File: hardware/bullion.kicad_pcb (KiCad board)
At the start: 2 copper layers, 14 parts, among them IC1 ATMEGA328P-A, P1 USB_OTG, P2 CONN_01X07, U1 SJ1-3524NG, U2 CH340G, Y1 Crystal

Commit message: v2.
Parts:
- moved C7 94.2 mm to (146.5, 90.6)
- moved Y1 94.2 mm to (145.0, 86.4)
- moved C2 94.2 mm to (123.1, 96.3)
- moved C3 94.2 mm to (135.6, 87.5)
- moved C4 94.2 mm to (154.6, 88.0)
- moved C5 94.2 mm to (123.2, 103.6)
- moved C8 94.2 mm to (146.3, 106.0)
- moved IC1 94.2 mm to (144.1, 98.5)
- moved P1 94.2 mm to (128.1, 113.7)
- moved P2 94.2 mm to (136.2, 113.2)
- moved R1 94.2 mm to (153.7, 96.3)
- moved U1 94.2 mm to (159.1, 111.6)
- moved U2 94.2 mm to (128.4, 98.4)
- moved C1 94.0 mm to (134.0, 97.3)
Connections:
- P2 pad 1: +5V -> GND
- P2 pad 2: GND -> +5V
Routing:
- net GND: track 59.6 -> 48.0 mm, vias 7 -> 5
- net +5V: track 97.9 -> 108.7 mm
- net Net-(C2-Pad1): track 80.3 -> 84.3 mm

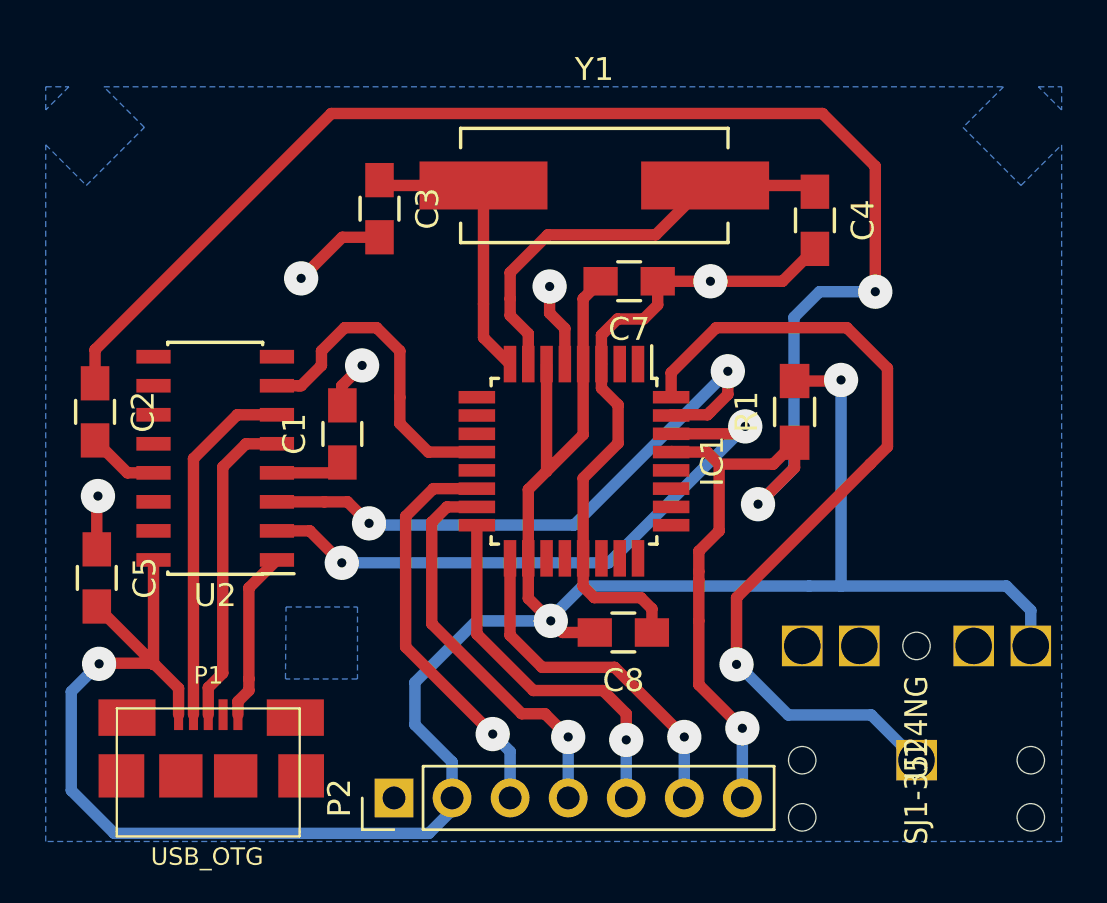
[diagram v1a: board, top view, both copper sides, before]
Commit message: Adding LEDs; fixing RS232 connection.
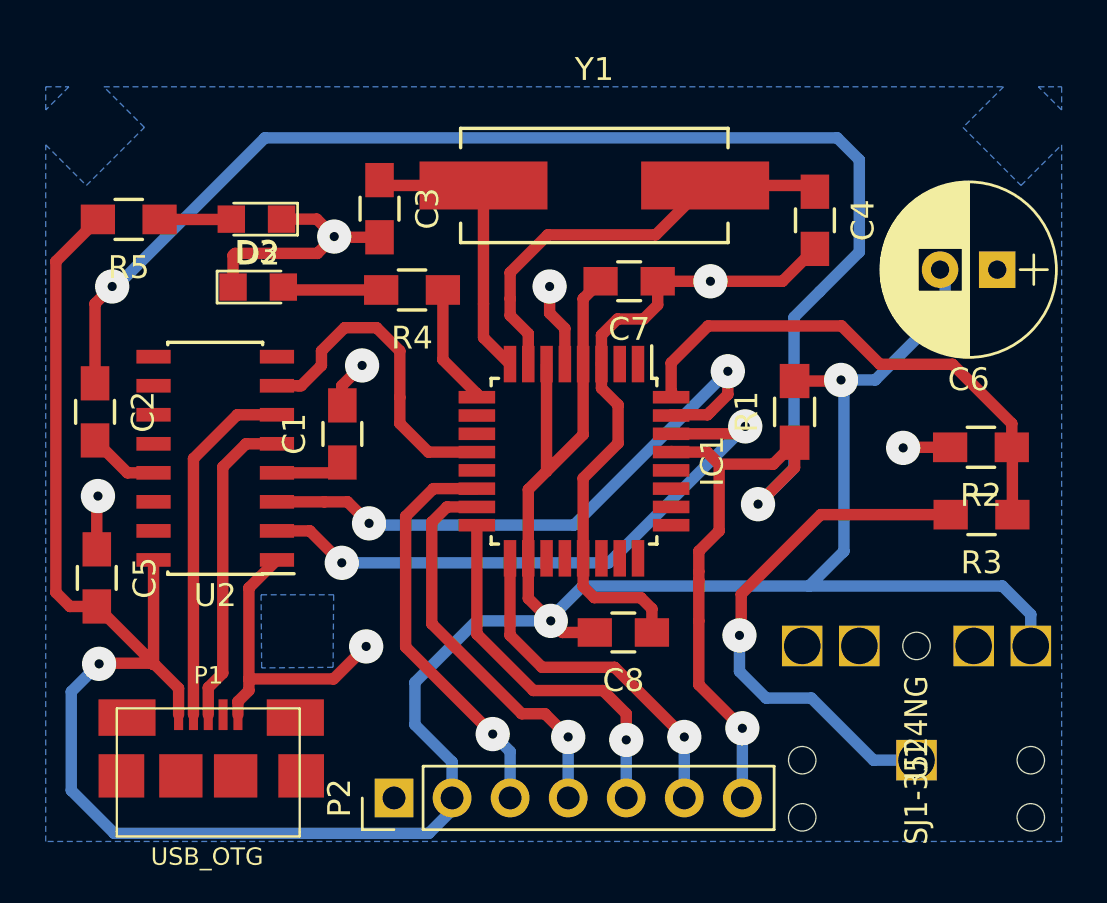
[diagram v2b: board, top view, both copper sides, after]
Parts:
- added C6: 47u, Capacitors_THT:CP_Radial_D7.5mm_P2.50mm, F.Cu at (162.6, 90.1)
- added D2: BLUE, LEDs:LED_0805, F.Cu at (130.3, 90.9)
- added D3: RED, LEDs:LED_0805, F.Cu at (130.2, 87.9)
- added R2: 2.2k, Resistors_SMD:R_0805_HandSoldering, F.Cu at (161.9, 97.9)
- added R3: 220, Resistors_SMD:R_0805_HandSoldering, F.Cu at (161.9, 100.8)
- added R4: 82, Resistors_SMD:R_0805_HandSoldering, F.Cu at (137.0, 91.0)
- added R5: 220, Resistors_SMD:R_0805_HandSoldering, F.Cu at (124.6, 87.9)
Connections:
- U1 pad 1: MM_TXD -> Net-(R3-Pad2)
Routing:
- net +5V: track 108.7 -> 136.0 mm
- net Net-(R3-Pad2): track 0.00 -> 23.4 mm, vias 0 -> 1
- net GND: track 48.0 -> 62.4 mm, vias 5 -> 7
- net MM_TXD: track 37.4 -> 23.1 mm, vias 1 -> 0
- net Net-(IC1-Pad9): track 0.00 -> 5.31 mm
- net Net-(D2-Pad2): track 0.00 -> 4.33 mm
- net Net-(D3-Pad2): track 0.00 -> 3.14 mm
- net Net-(C2-Pad1): track 84.3 -> 82.4 mm

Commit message: Updating hardware to latest revision; adding readme.
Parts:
- R5: value 220 -> 4.7k
- moved C6 2.31 mm to (160.3, 90.2), turned to 0 degrees
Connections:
- C6 pad 1: GND -> +5V
- C6 pad 2: +5V -> GND
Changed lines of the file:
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@@
   )
   (module Capacitors_THT:CP_Radial_D7.5mm_P2.50mm (layer F.Cu)
-    (at 162.6108 90.1192 180)
+    (at 160.2994 90.1954)
     (descr "CP, Radial series, Radial, pin pitch=2.50mm, , diameter=7.5mm, Electrolytic Capacitor")
     (tags "CP Radial series Radial pin pitch 2.50mm  diameter 7.5mm Electrolytic Capacitor")
-    (fp_text reference C6 (at 1.25 -4.81 180) (layer F.SilkS)
-      (effects (font (size 1 1) (thickness 0.15)))
-    )
-    (fp_text value 47u (at 1.25 4.81 180) (layer F.Fab)
+    (fp_text reference C6 (at 1.25 -4.81) (layer F.SilkS)
+      (effects (font (size 1 1) (thickness 0.15)))
+    )
+    (fp_text value 47u (at 1.25 4.81) (layer F.Fab)
       (effects (font (size 1 1) (thickness 0.15)))
     )
@@
     (fp_circle (center 1.25 0) (end 5.09 0) (layer F.SilkS) (width 0.12))
     (fp_circle (center 1.25 0) (end 5 0) (layer F.Fab) (width 0.1))
-    (pad 2 thru_hole circle (at 2.5 0 180) (size 1.6 1.6) (drill 0.8) (layers *.Cu *.Mask)
-      (net 2 +5V))
-    (pad 1 thru_hole rect (at 0 0 180) (size 1.6 1.6) (drill 0.8) (layers *.Cu *.Mask)
-      (net 8 GND))
+    (pad 2 thru_hole circle (at 2.5 0) (size 1.6 1.6) (drill 0.8) (layers *.Cu *.Mask)
+      (net 8 GND))
+    (pad 1 thru_hole rect (at 0 0) (size 1.6 1.6) (drill 0.8) (layers *.Cu *.Mask)
+      (net 2 +5V))
     (model Capacitors_ThroughHole.3dshapes/CP_Radial_D7.5mm_P2.50mm.wrl
       (at (xyz 0 0 0))
@@
       (effects (font (size 1 1) (thickness 0.15)))
     )
-    (fp_text value 220 (at 0 2.1 180) (layer F.Fab)
+    (fp_text value 4.7k (at 0 2.1 180) (layer F.Fab)
       (effects (font (size 1 1) (thickness 0.15)))
     )
@@
   (segment (start 164.0802 105.203) (end 164.0802 106.5822) (width 0.5) (layer B.Cu) (net 2))
   (segment (start 162.8394 103.9622) (end 164.0802 105.203) (width 0.5) (layer B.Cu) (net 2))
-  (segment (start 155.7782 94.9452) (end 157.2768 94.9452) (width 0.5) (layer B.Cu) (net 2))
-  (segment (start 160.3314 91.8906) (end 160.3314 90.0684) (width 0.5) (layer B.Cu) (net 2))
-  (segment (start 157.2768 94.9452) (end 160.3314 91.8906) (width 0.5) (layer B.Cu) (net 2))
   (segment (start 154.3812 103.9622) (end 155.8671 102.4763) (width 0.5) (layer B.Cu) (net 2))
   (segment (start 155.8671 102.4763) (end 155.9052 102.4382) (width 0.5) (layer B.Cu) (net 2))
@@
   (segment (start 126.79426 109.59084) (end 126.79426 108.43546) (width 0.5) (layer F.Cu) (net 2))
   (segment (start 126.79426 108.43546) (end 125.6792 107.3204) (width 0.5) (layer F.Cu) (net 2))
+  (segment (start 155.7782 94.9452) (end 157.2768 94.9452) (width 0.5) (layer B.Cu) (net 2))
+  (segment (start 160.3314 91.8906) (end 160.3314 90.0684) (width 0.5) (layer B.Cu) (net 2))
+  (segment (start 157.2768 94.9452) (end 160.3314 91.8906) (width 0.5) (layer B.Cu) (net 2))
   (segment (start 163.2496 97.8916) (end 163.2496 96.854) (width 0.5) (layer F.Cu) (net 4))
   (segment (start 148.3442 94.2004) (end 148.3442 95.7012) (width 0.5) (layer F.Cu) (net 4))
